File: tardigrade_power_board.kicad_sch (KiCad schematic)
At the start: 1 part, among them J1 Conn_01x04_Socket

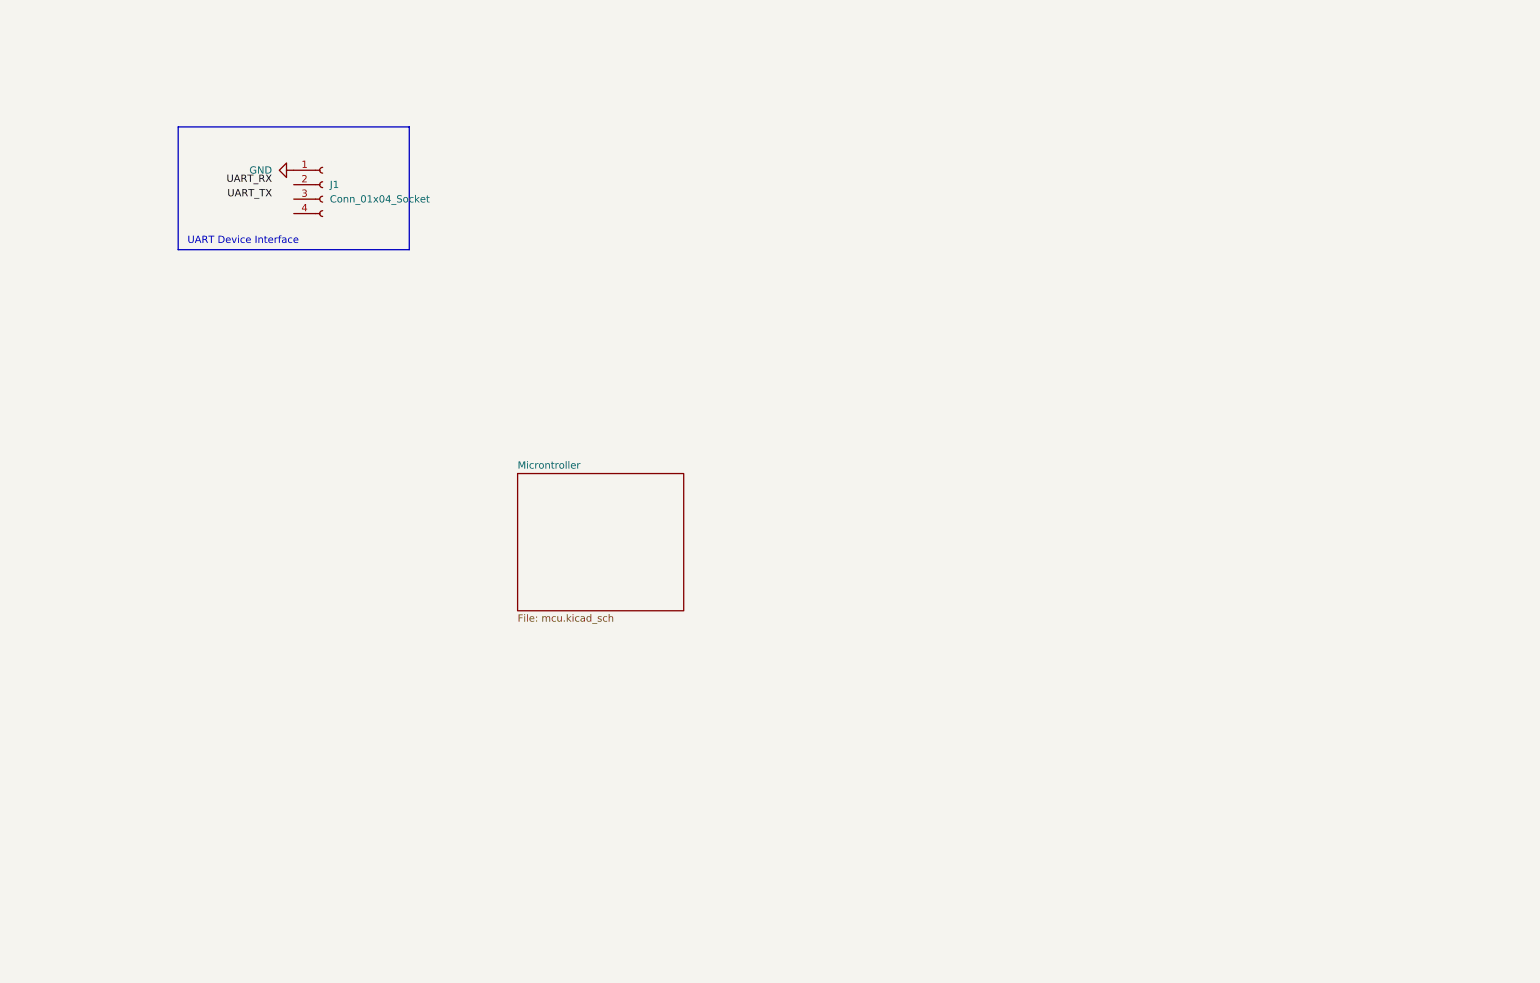
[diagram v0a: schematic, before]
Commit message: added 5v power supplies, 12v LDO, connectors, etc.
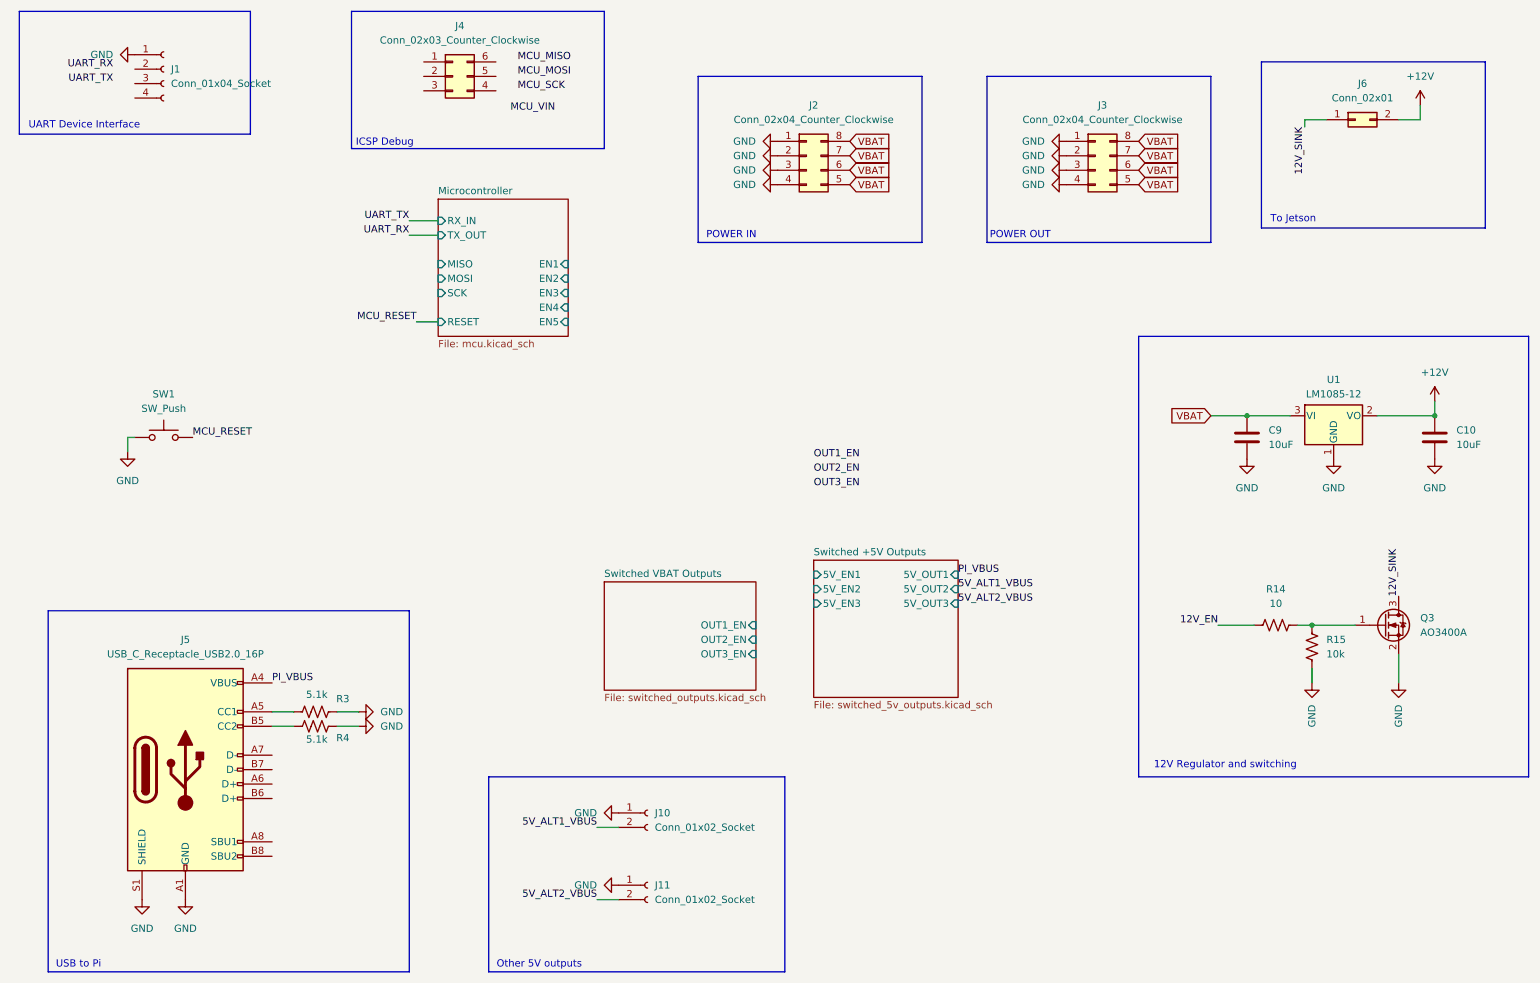
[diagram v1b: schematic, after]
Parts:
- added C10, C9: 10uF, Capacitor_SMD:C_0805_2012Metric_Pad1.18x1.45mm_HandSolder, symbol Device:C
- added J10, J11: Conn_01x02_Socket, Connector_JST:JST_PH_S2B-PH-K_1x02_P2.00mm_Horizontal, symbol Connector:Conn_01x02_Socket
- added J2, J3: Conn_02x04_Counter_Clockwise, Connector_Molex:Molex_Mini-Fit_Jr_5569-08A2_2x04_P4.20mm_Horizontal, symbol Connector_Generic:Conn_02x04_Counter_Clockwise
- added J4: Conn_02x03_Counter_Clockwise, Connector_PinHeader_2.54mm:PinHeader_2x03_P2.54mm_Vertical, symbol Connector_Generic:Conn_02x03_Counter_Clockwise
- added J5: USB_C_Receptacle_USB2.0_16P, Connector_USB:USB_C_Receptacle_GCT_USB4110, symbol Connector:USB_C_Receptacle_USB2.0_16P
- added J6: Conn_02x01, Connector_Molex:Molex_Mini-Fit_Jr_5569-02A2_2x01_P4.20mm_Horizontal, symbol Connector_Generic:Conn_02x01
- added Q3: AO3400A, Package_TO_SOT_SMD:SOT-23, symbol Transistor_FET:AO3400A
- added R14: 10, Resistor_SMD:R_0805_2012Metric_Pad1.20x1.40mm_HandSolder, symbol Device:R_US
- added R15: 10k, Resistor_SMD:R_0805_2012Metric_Pad1.20x1.40mm_HandSolder, symbol Device:R_US
- added R3, R4: 5.1k, Resistor_SMD:R_0805_2012Metric_Pad1.20x1.40mm_HandSolder, symbol Device:R_US
- added SW1: SW_Push, symbol Switch:SW_Push
- added U1: LM1085-12, Package_TO_SOT_SMD:TO-263-3_TabPin2, symbol Regulator_Linear:LM1085-12
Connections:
- net GND: now also C10.2, C9.2, J10.1 (Pin_1), J11.1 (Pin_1), J2.1 (Pin_1), J2.2 (Pin_2), J2.3 (Pin_3), J2.4 (Pin_4), J3.1 (Pin_1), J3.2 (Pin_2), J3.3 (Pin_3), J3.4 (Pin_4), J5.A1 (GND), J5.A12 (GND), J5.B1 (GND), J5.B12 (GND), J5.S1 (SHIELD), Q3.2 (S), R15.2, R3.2, R4.2, SW1.1, U1.1 (GND)
- new net: Q3.1 (G), R14.2, R15.1
- new net: J5.B5 (CC2), R4.1
- new net: J5.A5 (CC1), R3.1
- new net +12V: C10.1, J6.2 (Pin_2), U1.2 (VO)
- new net 12V_EN: R14.1
- new net 12V_SINK: J6.1 (Pin_1), Q3.3 (D)
- new net 5V_ALT1_VBUS: J10.2 (Pin_2)
- new net 5V_ALT2_VBUS: J11.2 (Pin_2)
- new net MCU_RESET: SW1.2
- new net PI_VBUS: J5.A4 (VBUS), J5.A9 (VBUS), J5.B4 (VBUS), J5.B9 (VBUS)
- new net VBAT: C9.1, J2.5 (Pin_5), J2.6 (Pin_6), J2.7 (Pin_7), J2.8 (Pin_8), J3.5 (Pin_5), J3.6 (Pin_6), J3.7 (Pin_7), J3.8 (Pin_8), U1.3 (VI)
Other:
- sheet Microntroller renamed Microcontroller
- added sheet Switched +5V Outputs (switched_5v_outputs.kicad_sch)
- added sheet Switched VBAT Outputs (switched_outputs.kicad_sch)
- sheet Microcontroller ports: added EN1, EN2, EN3, EN4, EN5, MISO, MOSI, RESET, RX_IN, SCK, TX_OUT; removed none
- note added: "12V Regulator and switching"
- note added: "ICSP Debug"
- note added: "Other 5V outputs"
- note added: "POWER IN"
- note added: "POWER OUT"
- note added: "To Jetson"
- note added: "USB to Pi"
- moved on the sheet: J1
